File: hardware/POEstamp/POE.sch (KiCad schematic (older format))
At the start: 122 parts, among them J1 0813-1X1T-57-F, J2 SWD, J3 MCU Port B, J4 MCU Port C, P1 PoE-, P2 PoE+, P3 GND, P4 +5V, P5 +12V, P6 +3V3, P7 12V_Switch, Q1 SI3440DV, NFET, Q2 MMBTA42, Q3 2N7002, Q4 MOSFET_N, SW1 reset, T1 PA1134, U1 LTC4267-3, U2 ENC28J60, U3 PS2811, U4 MCP16301, U5 TPS61175, U6 STM32F100RC

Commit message: Quite a handful of changes to the POEstamp hardware as a start: * Removed all of the extra components from copying the POE files. * Fixed a couple of incorrect components in the schematic. * Fixed the footprint for the LTC4267. It now uses a generated IP7351 footprint. * Updated the project file to match newer kicad symbol library organization. Need to do this to the other hardware files.
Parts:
- removed C10, C11: 10nF, Capacitors_SMD:c_0603, symbol capacitor
- removed C16, C18: 10uF, Capacitors_SMD:c_1206, symbol capacitor
- removed C17, C22, C24, C25: 10uF, Capacitors_SMD:c_0805, symbol capacitor
- removed C19, C26, C27, C28, C29, C30, C32, C33, C34, C35, C36, C38, C39: 100nF, Capacitors_SMD:c_0603, symbol capacitor
- removed C20: 47nF, Capacitors_SMD:c_0805, symbol capacitor
- removed C21: 180nF, Capacitors_SMD:c_0805, symbol capacitor
- removed C23: 22uF, Capacitors_SMD:c_0805, symbol capacitor
- removed C31, C37: 1uF, Capacitors_SMD:c_0603, symbol capacitor
- removed D10, D11: LED, LEDs:LED-0603, symbol LED-RESCUE-POE
- removed D13: 1N5189, rfid:SOD-123, symbol DIODESCH
- removed D14: 1N4148, rfid:SOD-123, symbol DIODE
- removed D15: MBRA340T3G, SMD_Packages:DO-214-AC_SMA, symbol DIODE
- removed D16: 12V LED, LEDs:LED-0603, symbol LED-RESCUE-POE
- removed D17: 3V3 LED, LEDs:LED-0603, symbol LED-RESCUE-POE
- removed D2: SMAJ58A, SMD_Packages:DO-214-AC_SMA, symbol DIODESCH
- removed G1: 25MHz OSC, rfid:Si501_2.5x2, symbol CMEMS_OSC
- removed G2: 24MHz OSC, rfid:Si501_2.5x2, symbol CMEMS_OSC
- removed J2: SWD, rfid:JST_PH_5pin, symbol CONN_5
- removed J3: MCU Port B, rfid:16_pin_breakout, symbol CONN_8X2
- removed J4: MCU Port C, rfid:16_pin_breakout, symbol CONN_8X2
- removed L2: choke, SMD_Packages:SMD-0805, symbol INDUCTOR_SMALL
- removed L3: 10uH, rfid:SRU1048, symbol INDUCTOR_SMALL
- removed L4: 15uH, rfid:NR6028, symbol INDUCTOR_SMALL
- removed P5: +12V, Connect:PINTST, symbol TST
- removed P6: +3V3, Connect:PINTST, symbol TST
- removed P7: 12V_Switch, rfid:SIL2-3.5mm, symbol CONN_2
- removed Q4: MOSFET_N, SMD_Packages:SOT-23-GDS, symbol MOSFET_N
- removed R15, R16, R18, R19: 49R9, SMD_Packages:SMD-0603, symbol resistor
- removed R17, R20: 1k, SMD_Packages:SMD-0603, symbol resistor
- removed R23: 226k, SMD_Packages:SMD-0603, symbol resistor
- removed R24: 1.4k, SMD_Packages:SMD-0805, symbol resistor
- removed R25: 31.2k, SMD_Packages:SMD-0603, symbol resistor
- removed R26, R29: 10k, SMD_Packages:SMD-0603, symbol resistor
- removed R27: 143k, SMD_Packages:SMD-0603, symbol resistor
- removed R28: 16.2k, SMD_Packages:SMD-0603, symbol resistor
- removed R30: 2.8k, SMD_Packages:SMD-0603, symbol resistor
- removed R31: 2.32k, SMD_Packages:SMD-0603, symbol resistor
- removed R32, R33: 24.9, SMD_Packages:SMD-0603, symbol resistor
- removed R34: 4.7k, SMD_Packages:SMD-0603, symbol resistor
- removed R35: 470R, SMD_Packages:SMD-0603, symbol R-RESCUE-POE
- removed R36: 10k, SMD_Packages:SMD-0603, symbol R-RESCUE-POE
- removed SW1: reset, rfid:TE-Switch-FSM-JSM, symbol SW_PUSH_4
- removed U2: ENC28J60, SMD_Packages:SSOP-28, symbol ENC28J60
- removed U4: MCP16301, SMD_Packages:SOT-23-6, symbol MCP16301
- removed U5: TPS61175, rfid:HTSSOP-14-1EP, symbol TPS61175
- removed U6: STM32F100RC, rfid:LQFP64, symbol STM32F100RC
- added D2: SMAJ58A, SMD_Packages:DO-214-AC_SMA, symbol ZENER
- D3, D4, D7: symbol DIODE -> DIODE-RESCUE-POE
- U1: footprint rfid:SSOP-16 -> IPC7351-Nominal:SOP63P600X175-16
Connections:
- net labels removed: 12V, 12VSwitch, 3V3, 3v3, EVDD, EVdd, EVddPLL, EVddRx, EVddTx, EthernetCS, EthernetINT, EthernetSCK, EthernetSI, EthernetSO, PB0, PB1, PB10, PB11, PB12, PB13, PB14, PB15, PB2, PB3, PB4, PB5, PB6, PB7, PB8, PB9, PC0, PC1, PC10, PC11, PC12, PC13, PC14, PC15, PC2, PC3, PC4, PC5, PC6, PC7, PC8, PC9, SWD_3V3, SWD_GND, VddOSC, VssOSC, nRST
- wire segments 428 -> 200
- no-connect marks 8 -> 1
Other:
- note removed: "5V to 12V@500mA boost supply"
- note removed: "5V to 3.3V@600mA buck supply"
- note removed: "Has internal pull up"
- note removed: "If clock stability issues arise pin 24\ncan be pulled down for lower noise."
- note removed: "Port B breakout connector"
- note removed: "Port C breakout connector"
- note removed: "Put the 1uF cap near the analog supply\n and the digital supply near it."
- note removed: "section 11.1 in the datasheet claims that most circuits \ndon't need a pull up on the reset pin. It has an internal \n(weak) pull up so this is not getting connected."
- moved on the sheet: C1, C12, C13, C14, C15, C2, C3, C4, C5, C6, C7, C8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

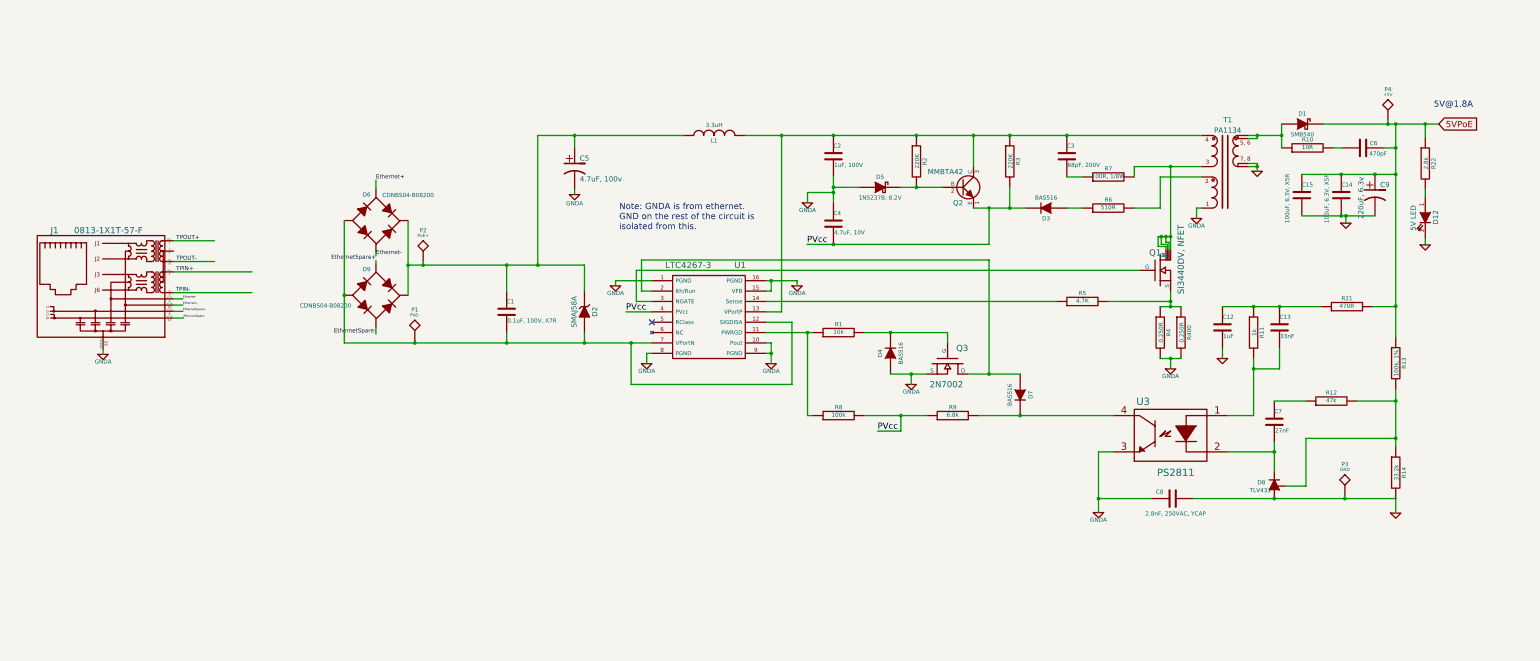
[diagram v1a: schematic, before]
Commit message: Significantly reorganized schematic. Labelled many of the sub sections in the circuit to try to provide better detail/understanding for layout.
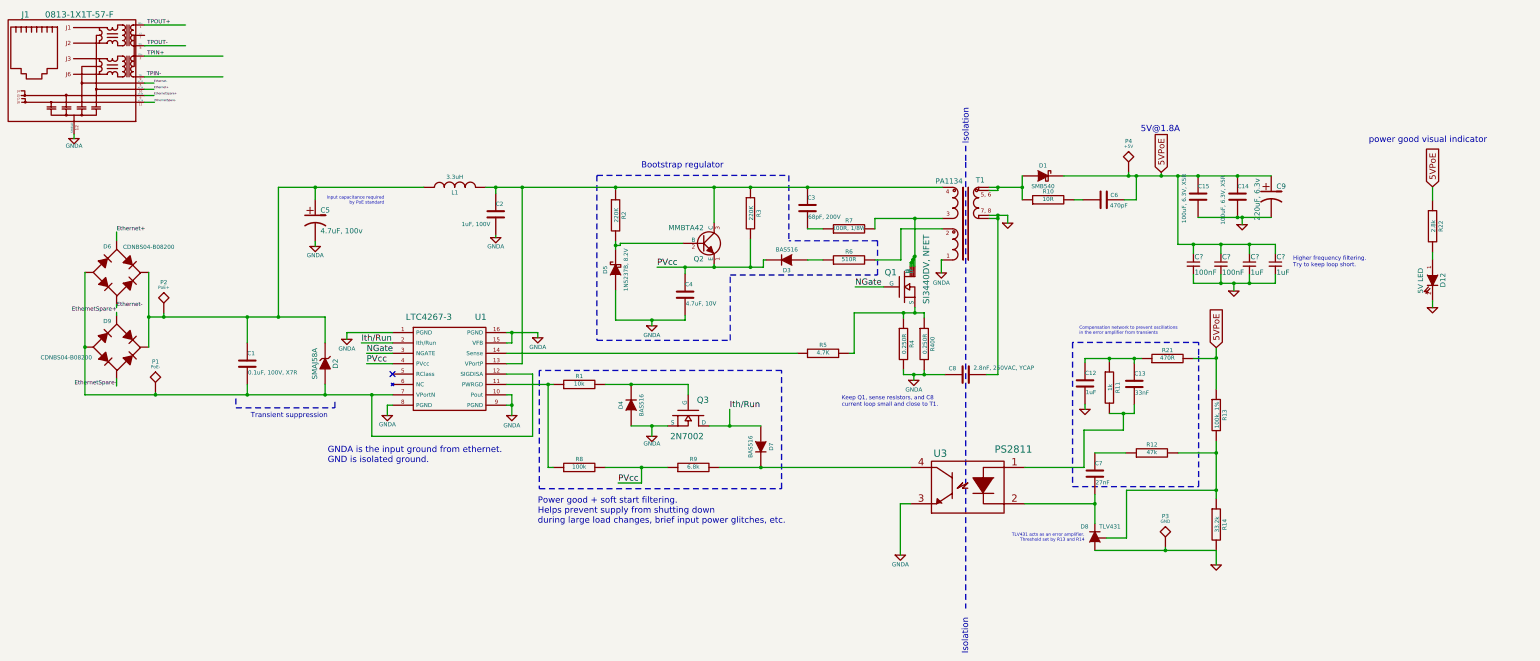
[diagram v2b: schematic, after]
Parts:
- added C? (x2): 100nF, symbol C_Small
- added C? (x2): 1uF, symbol C_Small
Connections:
- net 5VPoE: now also C?.1, C?.1, C?.1, C?.1; no longer R21.2
- net GND: now also C8.1, C?.2, C?.2, C?.2, C?.2; no longer C8.2
- net GNDA: now also C4.2, C8.2; no longer C4.1, C8.1
- net PVcc: now also C4.1; no longer C4.2
- net Ith/Run: now reaches D7.1 (A), Q3.D, U1.2 (Ith/Run)
- net NGate: now reaches Q1.3 (G), U1.3 (NGATE)
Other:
- note added: "Bootstrap regulator"
- note added: "Compensation network to prevent oscillations \nin the error amplifier from transients"
- note added: "GNDA is the input ground from ethernet.\nGND is isolated ground."
- note added: "Higher frequency filtering.\nTry to keep loop short."
- note added: "Input capacitance required \nby PoE standard"
- note added: "Isolation"
- note added: "Keep Q1, sense resistors, and C8 \ncurrent loop small and close to T1."
- note added: "Power good + soft start filtering. \nHelps prevent supply from shutting down \nduring large load changes, brief input power glitches, etc."
- note added: "TLV431 acts as an error amplifier.\nThreshold set by R13 and R14"
- note added: "Transient suppression"
- note added: "power good visual indicator"
- note removed: "Note: GNDA is from ethernet. \nGND on the rest of the circuit is\nisolated from this."
- moved on the sheet: C1, C12, C13, C14, C15, C2, C3, C4, C5, C6, C7, C8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

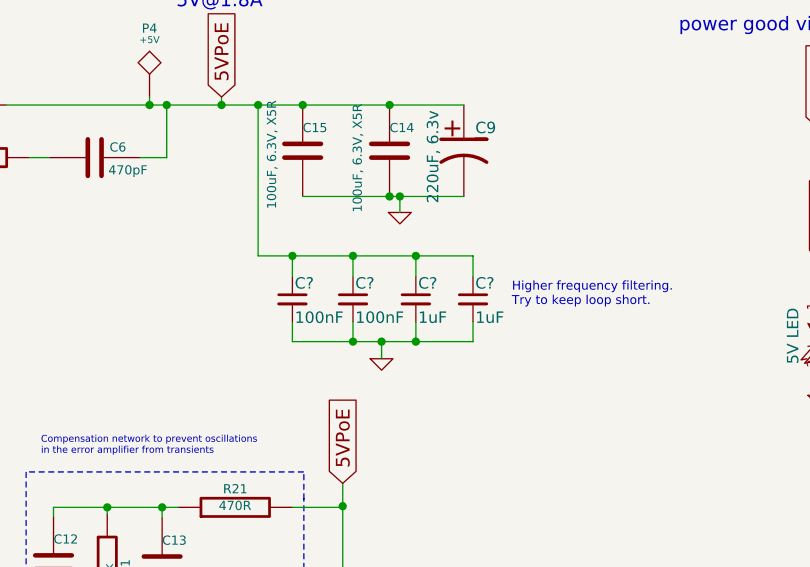
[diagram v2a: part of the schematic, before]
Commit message: Generated new netlist.
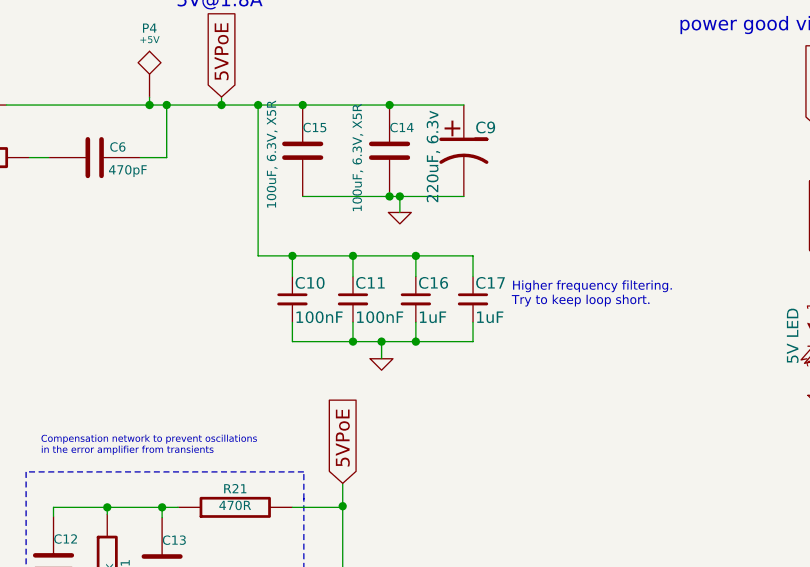
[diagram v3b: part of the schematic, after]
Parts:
- gave numbers to parts that had none: 4
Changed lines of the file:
@@
 $EndComp
 $Comp
-L GNDA-RESCUE-POE #PWR01
+L GNDA-RESCUE-POE #PWR5
 U 1 1 52997EAC
 P 5445 3150
-F 0 "#PWR01" H 5445 3150 40  0001 C CNN
+F 0 "#PWR5" H 5445 3150 40  0001 C CNN
 F 1 "GNDA" H 5445 3065 40  0000 C CNN
 F 2 "" H 5445 3150 60  0000 C CNN
@@
 $EndComp
 $Comp
-L GNDA-RESCUE-POE #PWR03
+L GNDA-RESCUE-POE #PWR11
 U 1 1 529988A9
 P 9475 4525
-F 0 "#PWR03" H 9475 4525 40  0001 C CNN
+F 0 "#PWR11" H 9475 4525 40  0001 C CNN
 F 1 "GNDA" H 9475 4435 40  0000 C CNN
 F 2 "" H 9475 4525 60  0000 C CNN
@@
 $EndComp
 $Comp
-L GNDA-RESCUE-POE #PWR04
+L GNDA-RESCUE-POE #PWR7
 U 1 1 52998B9C
 P 5850 4115
-F 0 "#PWR04" H 5850 4115 40  0001 C CNN
+F 0 "#PWR7" H 5850 4115 40  0001 C CNN
 F 1 "GNDA" H 5850 4025 40  0000 C CNN
 F 2 "" H 5850 4115 60  0000 C CNN
@@
 $EndComp
 $Comp
-L GNDA-RESCUE-POE #PWR05
+L GNDA-RESCUE-POE #PWR3
 U 1 1 52998BB0
 P 4010 4130
-F 0 "#PWR05" H 4010 4130 40  0001 C CNN
+F 0 "#PWR3" H 4010 4130 40  0001 C CNN
 F 1 "GNDA" H 4010 4040 40  0000 C CNN
 F 2 "" H 4010 4130 60  0000 C CNN
@@
 $EndComp
 $Comp
-L GNDA-RESCUE-POE #PWR06
+L GNDA-RESCUE-POE #PWR4
 U 1 1 52998BC4
 P 4400 4865
-F 0 "#PWR06" H 4400 4865 40  0001 C CNN
+F 0 "#PWR4" H 4400 4865 40  0001 C CNN
 F 1 "GNDA" H 4400 4780 40  0000 C CNN
 F 2 "" H 4400 4865 60  0000 C CNN
@@
 $EndComp
 $Comp
-L GNDA-RESCUE-POE #PWR07
+L GNDA-RESCUE-POE #PWR6
 U 1 1 52998BD8
 P 5600 4865
-F 0 "#PWR07" H 5600 4865 40  0001 C CNN
+F 0 "#PWR6" H 5600 4865 40  0001 C CNN
 F 1 "GNDA" H 5600 4770 40  0000 C CNN
 F 2 "" H 5600 4865 60  0000 C CNN
@@
 $EndComp
 $Comp
-L GNDA-RESCUE-POE #PWR08
+L GNDA-RESCUE-POE #PWR9
 U 1 1 529FE8B5
 P 6950 5065
-F 0 "#PWR08" H 6950 5065 40  0001 C CNN
+F 0 "#PWR9" H 6950 5065 40  0001 C CNN
 F 1 "GNDA" H 6950 4995 40  0000 C CNN
 F 2 "" H 6950 5065 60  0000 C CNN
@@
 $EndComp
 $Comp
-L GNDA-RESCUE-POE #PWR09
+L GNDA-RESCUE-POE #PWR10
 U 1 1 529FF2D9
 P 9345 6210
-F 0 "#PWR09" H 9345 6210 40  0001 C CNN
+F 0 "#PWR10" H 9345 6210 40  0001 C CNN
 F 1 "GNDA" H 9345 6120 40  0000 C CNN
 F 2 "" H 9345 6210 60  0000 C CNN
@@
 $EndComp
 $Comp
-L GND-RESCUE-POE #PWR010
+L GND-RESCUE-POE #PWR13
 U 1 1 529FF9B6
 P 10380 3010
-F 0 "#PWR010" H 10380 3010 30  0001 C CNN
+F 0 "#PWR13" H 10380 3010 30  0001 C CNN
 F 1 "GND" H 10380 2940 30  0001 C CNN
 F 2 "" H 10380 3010 60  0000 C CNN
@@
 $EndComp
 $Comp
-L GND-RESCUE-POE #PWR011
+L GND-RESCUE-POE #PWR17
 U 1 1 52A00211
 P 12640 3025
-F 0 "#PWR011" H 12640 3025 30  0001 C CNN
+F 0 "#PWR17" H 12640 3025 30  0001 C CNN
 F 1 "GND" H 12640 2955 30  0001 C CNN
 F 2 "" H 12640 3025 60  0000 C CNN
@@
 $EndComp
 $Comp
-L GND-RESCUE-POE #PWR012
+L GND-RESCUE-POE #PWR15
 U 1 1 52A252C8
 P 12390 6305
-F 0 "#PWR012" H 12390 6305 30  0001 C CNN
+F 0 "#PWR15" H 12390 6305 30  0001 C CNN
 F 1 "GND" H 12390 6235 30  0001 C CNN
 F 2 "" H 12390 6305 60  0000 C CNN
@@
 $EndComp
 $Comp
-L GND-RESCUE-POE #PWR013
+L GND-RESCUE-POE #PWR14
 U 1 1 52A263CC
 P 11125 4805
-F 0 "#PWR013" H 11125 4805 30  0001 C CNN
+F 0 "#PWR14" H 11125 4805 30  0001 C CNN
 F 1 "GND" H 11125 4735 30  0001 C CNN
 F 2 "" H 11125 4805 60  0000 C CNN
@@
 $EndComp
 $Comp
-L GND-RESCUE-POE #PWR014
+L GND-RESCUE-POE #PWR18
 U 1 1 52A27D1F
 P 14475 3825
-F 0 "#PWR014" H 14475 3825 30  0001 C CNN
+F 0 "#PWR18" H 14475 3825 30  0001 C CNN
 F 1 "GND" H 14475 3755 30  0001 C CNN
 F 2 "" H 14475 3825 60  0000 C CNN
@@
 EthernetSpare+
 $Comp
-L GNDA-RESCUE-POE #PWR017
+L GNDA-RESCUE-POE #PWR1
 U 1 1 52A3BB6D
 P 1380 2195
-F 0 "#PWR017" H 1380 2195 40  0001 C CNN
+F 0 "#PWR1" H 1380 2195 40  0001 C CNN
 F 1 "GNDA" H 1380 2125 40  0000 C CNN
 F 2 "" H 1380 2195 60  0000 C CNN
@@
 $EndComp
 $Comp
-L GNDA-RESCUE-POE #PWR?
+L GNDA-RESCUE-POE #PWR2
 U 1 1 54332B1C
 P 3705 3235
-F 0 "#PWR?" H 3705 3235 40  0001 C CNN
+F 0 "#PWR2" H 3705 3235 40  0001 C CNN
 F 1 "GNDA" H 3705 3150 40  0000 C CNN
 F 2 "" H 3705 3235 60  0000 C CNN
@@
 power good visual indicator
 $Comp
-L GNDA-RESCUE-POE #PWR02
+L GNDA-RESCUE-POE #PWR12
 U 1 1 52998525
 P 9740 3490
-F 0 "#PWR02" H 9740 3490 40  0001 C CNN
+F 0 "#PWR12" H 9740 3490 40  0001 C CNN
 F 1 "GNDA" H 9740 3395 40  0000 C CNN
 F 2 "" H 9740 3490 60  0000 C CNN
@@
 Connection ~ 7270 3435
 $Comp
-L GNDA-RESCUE-POE #PWR?
+L GNDA-RESCUE-POE #PWR8
 U 1 1 5653700A
 P 6950 4000
-F 0 "#PWR?" H 6950 4000 40  0001 C CNN
+F 0 "#PWR8" H 6950 4000 40  0001 C CNN
 F 1 "GNDA" H 6950 3910 40  0000 C CNN
 F 2 "" H 6950 4000 60  0000 C CNN
@@
 Connection ~ 12215 2555
 $Comp
-L C_Small C?
+L C_Small C10
 U 1 1 5653E810
 P 12170 3405
-F 0 "C?" H 12180 3475 50  0000 L CNN
+F 0 "C10" H 12180 3475 50  0000 L CNN
 F 1 "100nF" H 12180 3325 50  0000 L CNN
 F 2 "" H 12170 3405 60  0000 C CNN
@@
 $EndComp
 $Comp
-L C_Small C?
+L C_Small C11
 U 1 1 5653ED3B
 P 12435 3405
-F 0 "C?" H 12445 3475 50  0000 L CNN
+F 0 "C11" H 12445 3475 50  0000 L CNN
 F 1 "100nF" H 12445 3325 50  0000 L CNN
 F 2 "" H 12435 3405 60  0000 C CNN
@@
 $EndComp
 $Comp
-L C_Small C?
+L C_Small C16
 U 1 1 5653EE1B
 P 12710 3405
-F 0 "C?" H 12720 3475 50  0000 L CNN
+F 0 "C16" H 12720 3475 50  0000 L CNN
 F 1 "1uF" H 12720 3325 50  0000 L CNN
 F 2 "" H 12710 3405 60  0000 C CNN
@@
 $EndComp
 $Comp
-L C_Small C?
+L C_Small C17
 U 1 1 5653EF0A
 P 12960 3405
-F 0 "C?" H 12970 3475 50  0000 L CNN
+F 0 "C17" H 12970 3475 50  0000 L CNN
 F 1 "1uF" H 12970 3325 50  0000 L CNN
 F 2 "" H 12960 3405 60  0000 C CNN
@@
 Connection ~ 12710 3590
 $Comp
-L GND-RESCUE-POE #PWR?
+L GND-RESCUE-POE #PWR16
 U 1 1 56540FE7
 P 12560 3665
-F 0 "#PWR?" H 12560 3665 30  0001 C CNN
+F 0 "#PWR16" H 12560 3665 30  0001 C CNN
 F 1 "GND" H 12560 3595 30  0001 C CNN
 F 2 "" H 12560 3665 60  0000 C CNN

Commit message: Included BOM info on everything except transistors. Updated many footprints to IPC footprints. Also added a SOD-128 footprint.
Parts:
- C1: footprint Capacitors_SMD:c_0805 -> IPC7351-Nominal:CAPC2012X95; Vend1 (none) -> digikey; Vend1Id (none) -> 1276-2447-1-ND
- C10, C11: footprint (none) -> IPC7351-Nominal:CAPC1608X90; Vend1 (none) -> Digikey; Vend1Id (none) -> 311-1343-1-ND
- C12: footprint Capacitors_SMD:c_0603 -> IPC7351-Nominal:CAPC1608X90; Vend1 (none) -> Digikey; Vend1Id (none) -> 1276-1041-1-ND
- C13: footprint Capacitors_SMD:c_0603 -> IPC7351-Nominal:CAPC1608X95; Vend1 (none) -> Digikey; Vend1Id (none) -> 445-5093-1-ND
- C14, C15: footprint Capacitors_SMD:c_1206 -> IPC7351-Nominal:CAPC3216X180; Vend1 (none) -> Digikey; Vend1Id (none) -> 399-5620-1-ND
- C16, C17: footprint (none) -> IPC7351-Nominal:CAPC1608X90; Vend1 (none) -> Digikey; Vend1Id (none) -> 490-3897-1-ND
- C2: footprint Capacitors_SMD:c_1206 -> IPC7351-Nominal:CAPC3216X180; Vend1 (none) -> Digikey; Vend1Id (none) -> 587-1777-1-ND
- C3: footprint Capacitors_SMD:c_0603 -> IPC7351-Nominal:CAPC1608X87; Vend1 (none) -> Digikey; Vend1Id (none) -> 399-10054-1-ND
- C4: footprint Capacitors_SMD:c_0805 -> IPC7351-Nominal:CAPC2012X135; Vend1 (none) -> Digikey; Vend1Id (none) -> 1276-1259-1-ND
- C5: Vend1 (none) -> Digikey; Vend1Id (none) -> PCE3972CT-ND
- C6: footprint Capacitors_SMD:c_0603 -> IPC7351-Nominal:CAPC1608X90; Vend1 (none) -> Digikey; Vend1Id (none) -> 1276-1094-1-ND
- C7: footprint Capacitors_SMD:c_0805 -> IPC7351-Nominal:CAPC2012X88; Vend1 (none) -> Digikey; Vend1Id (none) -> 311-1139-1-ND
- C8: footprint rfid:kemet_C900 -> IPC7351-Nominal:CAPC4532X150; Vend1 (none) -> Digikey; Vend1Id (none) -> 490-3492-1-ND
- C9: Vend1 (none) -> Digikey; Vend1Id (none) -> PCE3766CT-ND
- D1: value SMB540 -> PMEG3050EP; footprint SMD_Packages:DO-214-AA_SMB -> rfid:SOD-128; Vend1 (none) -> Digikey; Vend1Id (none) -> 568-6753-1-ND
- D12: Vend1 (none) -> Digikey; Vend1Id (none) -> 475-1409-1-ND
- D2: footprint SMD_Packages:DO-214-AC_SMA -> IPC7351-Nominal:DIOM5436X265; BOM DIO SMD SMAJ58A [DO-214-AC] -> (none); Vend1 (none) -> Digikey; Vend1Id (none) -> SMAJ58ALFCT-ND
- D3, D4, D7: Vend1 (none) -> Digikey; Vend1Id (none) -> 568-1603-1-ND
- D5: Vend1 (none) -> Digikey; Vend1Id (none) -> BZT52C8V2-FDICT-ND
- D6: Vend1 (none) -> Digikey; Vend1Id (none) -> CDNBS04-B08200CT-ND
- D8: footprint SMD_Packages:SOT-23 -> smd-semi:SOT-23; Vend1 (none) -> Digikey; Vend1Id (none) -> TLV431AFTACT-ND
- L1: footprint SMD_Packages:SMD-0805 -> IPC7351-Nominal:INDC2012X130; Vend1 (none) -> Digikey; Vend1id (none) -> 445-6394-1-ND
- R1: footprint SMD_Packages:SMD-0603 -> IPC7351-Nominal:RESC1608X55; Vend1 (none) -> Digikey; Vend1Id (none) -> P10.0KHCT-ND
- R10: footprint SMD_Packages:SMD-0603 -> IPC7351-Nominal:RESC1608X55; Vend1 (none) -> Digikey; Vend1Id (none) -> P10GCT-ND
- R11: footprint SMD_Packages:SMD-0603 -> IPC7351-Nominal:RESC1608X55; Vend1 (none) -> Digikey; Vend1Id (none) -> A106049CT-ND
- R12: footprint SMD_Packages:SMD-0603 -> IPC7351-Nominal:RESC1608X55; Vend1 (none) -> Digikey; Vend1Id (none) -> P47.0KHCT-ND
- R13, R8: footprint SMD_Packages:SMD-0603 -> IPC7351-Nominal:RESC1608X55; Vend1 (none) -> Digikey; Vend1Id (none) -> P100KHCT-ND
- R14: footprint SMD_Packages:SMD-0603 -> IPC7351-Nominal:RESC1608X55; Vend1 (none) -> Digikey; Vend1Id (none) -> P33.2KHCT-ND
- R2: footprint SMD_Packages:SMD-0603 -> IPC7351-Nominal:RESC1608X55; Vend1 (none) -> Digikey; VendId1 (none) -> P220KHCT-ND
- R21: footprint SMD_Packages:SMD-0603 -> IPC7351-Nominal:RESC1608X55; Vend1 (none) -> Digikey; Vend1Id (none) -> P470HCT-ND
- R22: footprint SMD_Packages:SMD-0603 -> IPC7351-Nominal:RESC1608X55; Vend1 (none) -> Digikey; Vend1Id (none) -> 311-2.80KHRCT-ND
- R3: footprint SMD_Packages:SMD-0603 -> IPC7351-Nominal:RESC1608X55; Vend1 (none) -> Digikey; Vend1Id (none) -> P220KHCT-ND
- R4, R400: footprint SMD_Packages:SMD-0805 -> IPC7351-Nominal:RESC2013X65; Vend1 (none) -> Digikey; Vend1Id (none) -> CSR0805FKR250CT-ND
- R5: footprint SMD_Packages:SMD-0603 -> IPC7351-Nominal:RESC1608X55; Vend1 (none) -> Digikey; Vend1Id (none) -> A106050CT-ND
- R6: footprint SMD_Packages:SMD-0603 -> IPC7351-Nominal:RESC1608X55; Vend1 (none) -> Digikey; Vend1Id (none) -> P510HCT-ND
- R7: footprint SMD_Packages:SMD-0805 -> IPC7351-Nominal:RESC2012X70; Vend1 (none) -> Digikey; Vend1Id (none) -> P100CCT-ND
- R9: footprint SMD_Packages:SMD-0603 -> IPC7351-Nominal:RESC1608X55; Vend1 (none) -> Digikey; Vend1Id (none) -> P6.80KHCT-ND
- U1: Vend1 (none) -> Digikey; Vend1Id (none) -> LTC4267CGN-3#PBF-ND
